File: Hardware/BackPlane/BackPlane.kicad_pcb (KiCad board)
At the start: 2 copper layers, 188 x 68.6 mm, 18 parts, among them J1 TO A6502, J2 Video, J4 FDC, J5 EX1, J6 EX2, J7 User Rom Enable, U1 74LS245, U2 74LS373, U3 74LS373, U4 74LS373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

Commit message: Update
Laying out tracks
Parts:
- moved C5 42.3 mm to (245.1, 109.2), turned to 270 degrees
- moved J7 28.4 mm to (245.1, 91.4)
- moved U5 7.18 mm to (236.2, 109.2)
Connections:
- J1 pad 10: /A1 -> /_A1
- J1 pad 11: /D4 -> /_D4
- J1 pad 12: /A2 -> /_A2
- J1 pad 13: /D5 -> /_D5
- J1 pad 14: /A3 -> /_A3
- J1 pad 15: /D6 -> /_D6
- J1 pad 16: /A4 -> /_A4
- J1 pad 17: /D7 -> /_D7
- J1 pad 18: /A5 -> /_A5
- J1 pad 19: /R~W -> /_R~W
- J1 pad 20: /A6 -> /_A6
- J1 pad 22: /A7 -> /_A7
- J1 pad 23: /~RESET -> /_~RESET
- J1 pad 24: /A8 -> /_A8
- J1 pad 26: /A9 -> /_A9
- J1 pad 27: /CLK -> /_CLK
- J1 pad 28: /A10 -> /_A10
- J1 pad 29: /C000 -> /_C000
- J1 pad 3: /D0 -> /_D0
- J1 pad 30: /A11 -> /_A11
- J1 pad 31: /6000 -> /_6000
- J1 pad 32: /A12 -> /_A12
- J1 pad 33: /4000 -> /_4000
- J1 pad 34: /A13 -> /_A13
- J1 pad 35: /2000 -> /_2000
- J1 pad 36: /A14 -> /_A14
- J1 pad 38: /A15 -> /_A15
- J1 pad 5: /D1 -> /_D1
- J1 pad 6: /RDY -> /_RDY
- J1 pad 7: /D2 -> /_D2
- J1 pad 8: /A0 -> /_A0
- J1 pad 9: /D3 -> /_D3
- J7 pad 2: GND -> Net-(J7-Pad2)
- U1 pad 2: /D0 -> /_D0
- U1 pad 3: /D1 -> /_D1
- U1 pad 4: /D2 -> /_D2
- U1 pad 5: /D3 -> /_D3
- U1 pad 6: /D4 -> /_D4
- U1 pad 7: /D5 -> /_D5
- U1 pad 8: /D6 -> /_D6
- U1 pad 9: /D7 -> /_D7
- U2 pad 11: /CLK -> /_CLK
- U2 pad 13: /A4 -> /_A4
- U2 pad 14: /A5 -> /_A5
- U2 pad 17: /A6 -> /_A6
- U2 pad 18: /A7 -> /_A7
- U2 pad 3: /A0 -> /_A0
- U2 pad 4: /A1 -> /_A1
- U2 pad 7: /A2 -> /_A2
- U2 pad 8: /A3 -> /_A3
- U3 pad 11: /CLK -> /_CLK
- U3 pad 13: /A12 -> /_A12
- U3 pad 14: /A13 -> /_A13
- U3 pad 17: /A14 -> /_A14
- U3 pad 18: /A15 -> /_A15
- U3 pad 3: /A8 -> /_A8
- U3 pad 4: /A9 -> /_A9
- U3 pad 7: /A10 -> /_A10
- U3 pad 8: /A11 -> /_A11
- U4 pad 11: /CLK -> /_CLK
- U4 pad 13: /C000 -> /_C000
- U4 pad 14: /6000 -> /_6000
- U4 pad 17: /4000 -> /_4000
- U4 pad 18: /2000 -> /_2000
- U4 pad 3: /R~W -> /_R~W
- U4 pad 4: /~RESET -> /_~RESET
- U4 pad 7: /RDY -> /_RDY
- U4 pad 8: /CLK -> /_CLK
- U5 pad 22: GND -> Net-(J7-Pad2)
- U6 pad 1: /R~W -> /_R~W
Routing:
- net /C000: track 43.1 -> 106.8 mm, vias 0 -> 1
- net /D0: track 66.7 -> 129.6 mm
- net /D1: track 66.7 -> 125.3 mm
- net /D2: track 66.7 -> 119.4 mm
- net /_A7: track 0.00 -> 48.3 mm
- net /_A6: track 0.00 -> 43.2 mm
- net /A10: track 66.7 -> 106.1 mm, vias 0 -> 2
- net /A13: track 66.7 -> 106.1 mm
- net /A11: track 66.7 -> 99.5 mm
- net /_A5: track 0.00 -> 31.8 mm
- net /_D6: track 0.00 -> 31.5 mm
- net /_D4: track 0.00 -> 31.5 mm
- net /A7: track 66.7 -> 98.2 mm
- net /A5: track 66.7 -> 98.2 mm
- net /A3: track 66.7 -> 98.2 mm
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
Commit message: Update
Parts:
- added J8: DB Enable select, Connector_PinHeader_2.54mm:PinHeader_1x03_P2.54mm_Vertical, F.Cu at (111.8, 69.8)
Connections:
- U1 pad 19: GND -> Net-(J8-Pad2)
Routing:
- net 5V: track 148.7 -> 506.8 mm
- net /A2: track 98.2 -> 214.8 mm, vias 0 -> 2
- net /_CLK: track 0.00 -> 95.5 mm
- net /A7: track 98.2 -> 171.4 mm, vias 0 -> 2
- net /A1: track 98.2 -> 164.8 mm, vias 0 -> 2
- net /A6: track 98.2 -> 162.7 mm, vias 0 -> 1
- net /A0: track 98.2 -> 162.3 mm, vias 0 -> 2
- net /R~W: track 113.7 -> 66.7 mm
- net /D5: track 88.6 -> 122.7 mm
- net /D3: track 88.6 -> 122.7 mm
- net /D2: track 119.4 -> 153.5 mm
- net /D7: track 88.6 -> 122.7 mm
- net /D6: track 88.6 -> 122.7 mm
- net /D4: track 88.6 -> 122.7 mm
- net /D1: track 125.3 -> 159.3 mm
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
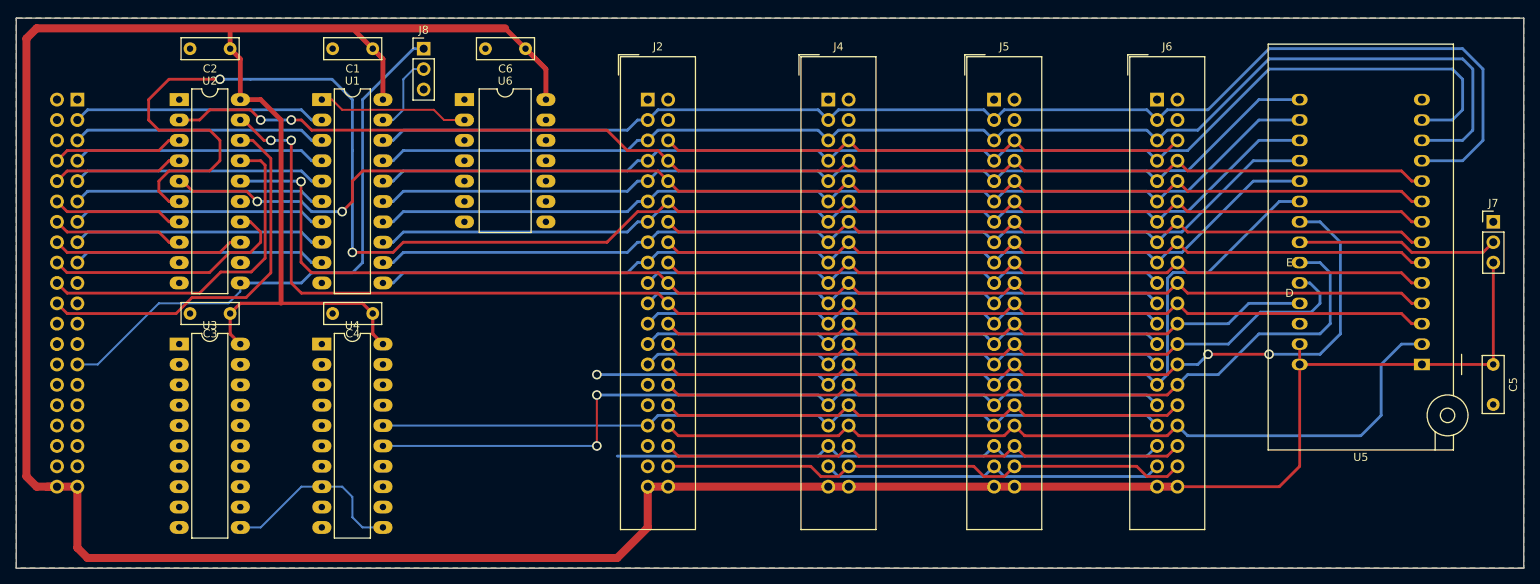
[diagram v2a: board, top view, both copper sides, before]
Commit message: update
Changed 74LS373 to 74LS573, added pull up resistors to input lines
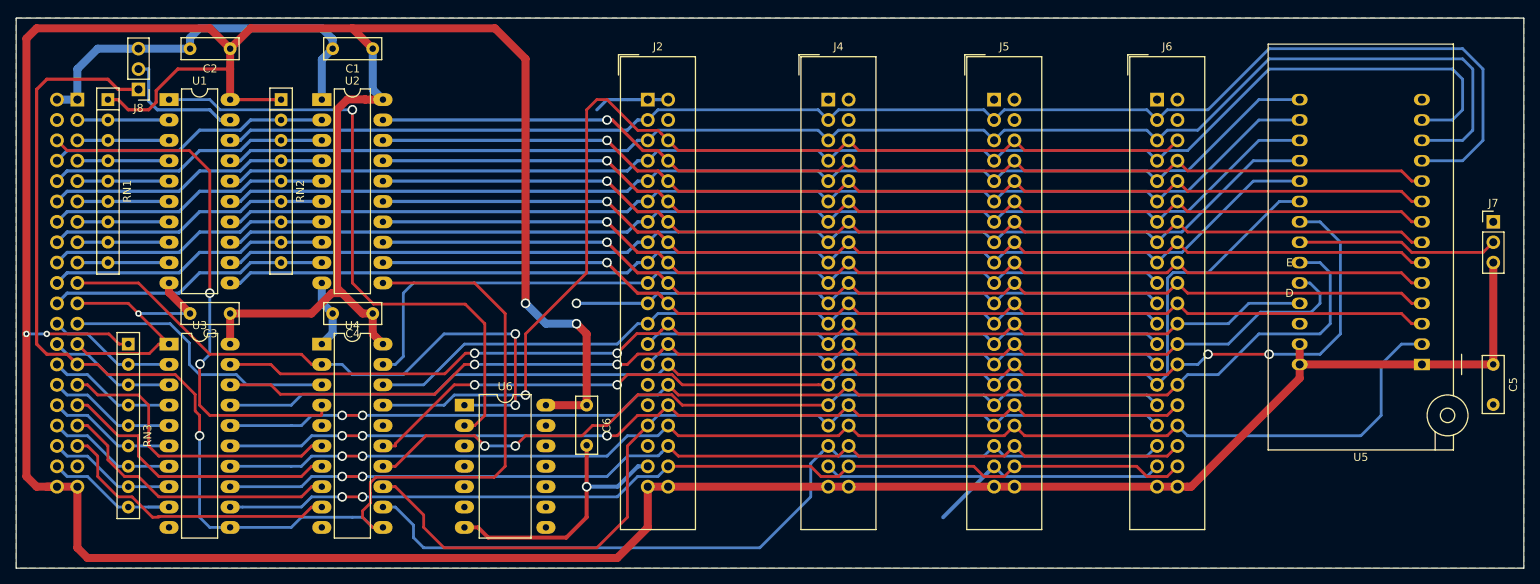
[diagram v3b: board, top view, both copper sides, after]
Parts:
- added RN1: R_Network08, Resistor_THT:R_Array_SIP9, F.Cu at (72.4, 76.2)
- added RN2: R_Network08, Resistor_THT:R_Array_SIP9, F.Cu at (94.0, 76.2)
- added RN3: R_Network08, Resistor_THT:R_Array_SIP9, F.Cu at (74.9, 106.7)
- U2, U3, U4: value 74LS373 -> 74LS573
- moved C6 45.1 mm to (132.1, 114.3), turned to 270 degrees
- moved U6 38.1 mm to (116.8, 114.3)
- moved J8 35.9 mm to (76.2, 74.9), turned to 180 degrees
- moved U1 19.0 mm to (80.0, 76.2)
- moved U2 17.8 mm to (99.1, 76.2)
- moved U3 1.27 mm to (80.0, 106.7)
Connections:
- U2 pad 12: /A4 -> /A7
- U2 pad 13: /_A4 -> /A6
- U2 pad 14: /_A5 -> /A5
- U2 pad 15: /A5 -> /A4
- U2 pad 16: /A6 -> /A3
- U2 pad 17: /_A6 -> /A2
- U2 pad 18: /_A7 -> /A1
- U2 pad 19: /A7 -> /A0
- U2 pad 2: /A0 -> /_A0
- U2 pad 3: /_A0 -> /_A1
- U2 pad 4: /_A1 -> /_A2
- U2 pad 5: /A1 -> /_A3
- U2 pad 6: /A2 -> /_A4
- U2 pad 7: /_A2 -> /_A5
- U2 pad 8: /_A3 -> /_A6
- U2 pad 9: /A3 -> /_A7
- U3 pad 12: /A12 -> /A15
- U3 pad 13: /_A12 -> /A14
- U3 pad 14: /_A13 -> /A13
- U3 pad 15: /A13 -> /A12
- U3 pad 16: /A14 -> /A11
- U3 pad 17: /_A14 -> /A10
- U3 pad 18: /_A15 -> /A9
- U3 pad 19: /A15 -> /A8
- U3 pad 2: /A8 -> /_A8
- U3 pad 3: /_A8 -> /_A9
- U3 pad 4: /_A9 -> /_A10
- U3 pad 5: /A9 -> /_A11
- U3 pad 6: /A10 -> /_A12
- U3 pad 7: /_A10 -> /_A13
- U3 pad 8: /_A11 -> /_A14
- U3 pad 9: /A11 -> /_A15
- U4 pad 12: /C000 -> /2000
- U4 pad 13: /_C000 -> /4000
- U4 pad 14: /_6000 -> /6000
- U4 pad 15: /6000 -> /C000
- U4 pad 16: /4000 -> (no net)
- U4 pad 17: /_4000 -> /RDY
- U4 pad 18: /_2000 -> /~RESET
- U4 pad 19: /2000 -> /R~W
- U4 pad 2: /R~W -> /_R~W
- U4 pad 3: /_R~W -> /_~RESET
- U4 pad 4: /_~RESET -> /_RDY
- U4 pad 5: /~RESET -> (no net)
- U4 pad 6: /RDY -> /_C000
- U4 pad 7: /_RDY -> /_6000
- U4 pad 8: /_CLK -> /_4000
- U4 pad 9: /CLK -> /_2000
- U6 pad 11: GND -> (no net)
- U6 pad 13: GND -> (no net)
- U6 pad 3: GND -> (no net)
- U6 pad 5: GND -> (no net)
- U6 pad 9: GND -> (no net)
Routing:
- net GND: track 176.4 -> 333.8 mm, vias 0 -> 3
- net /A2: track 214.8 -> 135.9 mm, vias 2 -> 1
- net /_R~W: track 0.00 -> 76.7 mm, vias 0 -> 2
- net /_CLK: track 95.5 -> 169.2 mm, vias 0 -> 1
- net /RDY: track 66.7 -> 136.5 mm, vias 0 -> 1
- net /_RDY: track 0.00 -> 67.3 mm, vias 0 -> 2
- net Net-(U1-Pad1): track 18.8 -> 78.1 mm, vias 0 -> 1
- net /A8: track 82.9 -> 140.6 mm, vias 0 -> 2
- net /A9: track 90.9 -> 148.6 mm, vias 0 -> 2
- net /A14: track 66.7 -> 123.4 mm, vias 0 -> 2
- net /A13: track 106.1 -> 162.8 mm, vias 0 -> 2
- net /A11: track 99.5 -> 156.3 mm, vias 0 -> 2
- net /A10: track 106.1 -> 162.8 mm
- net /A15: track 66.7 -> 123.4 mm, vias 0 -> 2
- net /A12: track 66.7 -> 123.4 mm, vias 0 -> 3
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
